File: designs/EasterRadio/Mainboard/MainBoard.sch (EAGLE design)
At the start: 83 parts, among them IC1 74HC595D, IC2 74HC595D, IC3 74HC595D, IC4 Analog Digital, IC6 CP2102, Q1 SS8050-G, Q2 SS8050-G

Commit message: checked Mainboard and esp32
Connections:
- net 3.3V: no longer GPIOS.5
- net CS2: now also GPIOS.5
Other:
- note added: "Mainboard"
- note added: "Revision 1 02.04.21"
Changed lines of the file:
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@@
 <plain>
 <frame x1="0" y1="0" x2="370.84" y2="337.82" columns="8" rows="5" layer="91"/>
+<text x="2.54" y="340.36" size="6.4516" layer="91">Mainboard</text>
+<text x="48.26" y="340.36" size="1.778" layer="91">Revision 1 02.04.21</text>
 </plain>
 <instances>
@@
 </instances>
 <busses>
-<bus name="SPI:CS,CS2,DC,GND,MOSI,RST,SCLK,SDA">
+<bus name="SPI:CS,DC,GND,MOSI,RST,SCLK,SDA">
 <segment>
 <wire x1="157.48" y1="177.8" x2="157.48" y2="154.94" width="0.762" layer="92"/>
@@
 <label x="218.44" y="96.52" size="1.778" layer="95"/>
 <pinref part="GPIOS" gate="A" pin="4"/>
-<pinref part="GPIOS" gate="A" pin="5"/>
-<wire x1="238.76" y1="93.98" x2="218.44" y2="93.98" width="0.1524" layer="91"/>
-<wire x1="218.44" y1="93.98" x2="218.44" y2="96.52" width="0.1524" layer="91"/>
-<pinref part="GPIOS" gate="A" pin="6"/>
-<wire x1="238.76" y1="91.44" x2="218.44" y2="91.44" width="0.1524" layer="91"/>
-<wire x1="218.44" y1="91.44" x2="218.44" y2="93.98" width="0.1524" layer="91"/>
-<junction x="218.44" y="93.98"/>
 </segment>
 <segment>
@@
 <label x="254" y="55.88" size="1.778" layer="95" rot="R90"/>
 <pinref part="AMPLIFIER" gate="A" pin="8"/>
+</segment>
+<segment>
+<pinref part="GPIOS" gate="A" pin="6"/>
+<wire x1="238.76" y1="91.44" x2="218.44" y2="91.44" width="0.1524" layer="91"/>
+<label x="218.44" y="91.44" size="1.778" layer="95"/>
 </segment>
 </net>
@@
 <segment>
 <pinref part="ESP32" gate="A" pin="10"/>
-<wire x1="180.34" y1="144.78" x2="213.36" y2="144.78" width="0.1524" layer="91"/>
+<wire x1="180.34" y1="144.78" x2="200.66" y2="144.78" width="0.1524" layer="91"/>
 <label x="200.66" y="144.78" size="1.778" layer="95" align="bottom-right"/>
-<wire x1="213.36" y1="144.78" x2="215.9" y2="142.24" width="0.1524" layer="91"/>
 </segment>
 <segment>
@@
 <label x="276.86" y="154.94" size="1.778" layer="95"/>
 </segment>
+<segment>
+<pinref part="GPIOS" gate="A" pin="5"/>
+<wire x1="238.76" y1="93.98" x2="218.44" y2="93.98" width="0.1524" layer="91"/>
+<label x="218.44" y="93.98" size="1.778" layer="95"/>
+</segment>
 </net>

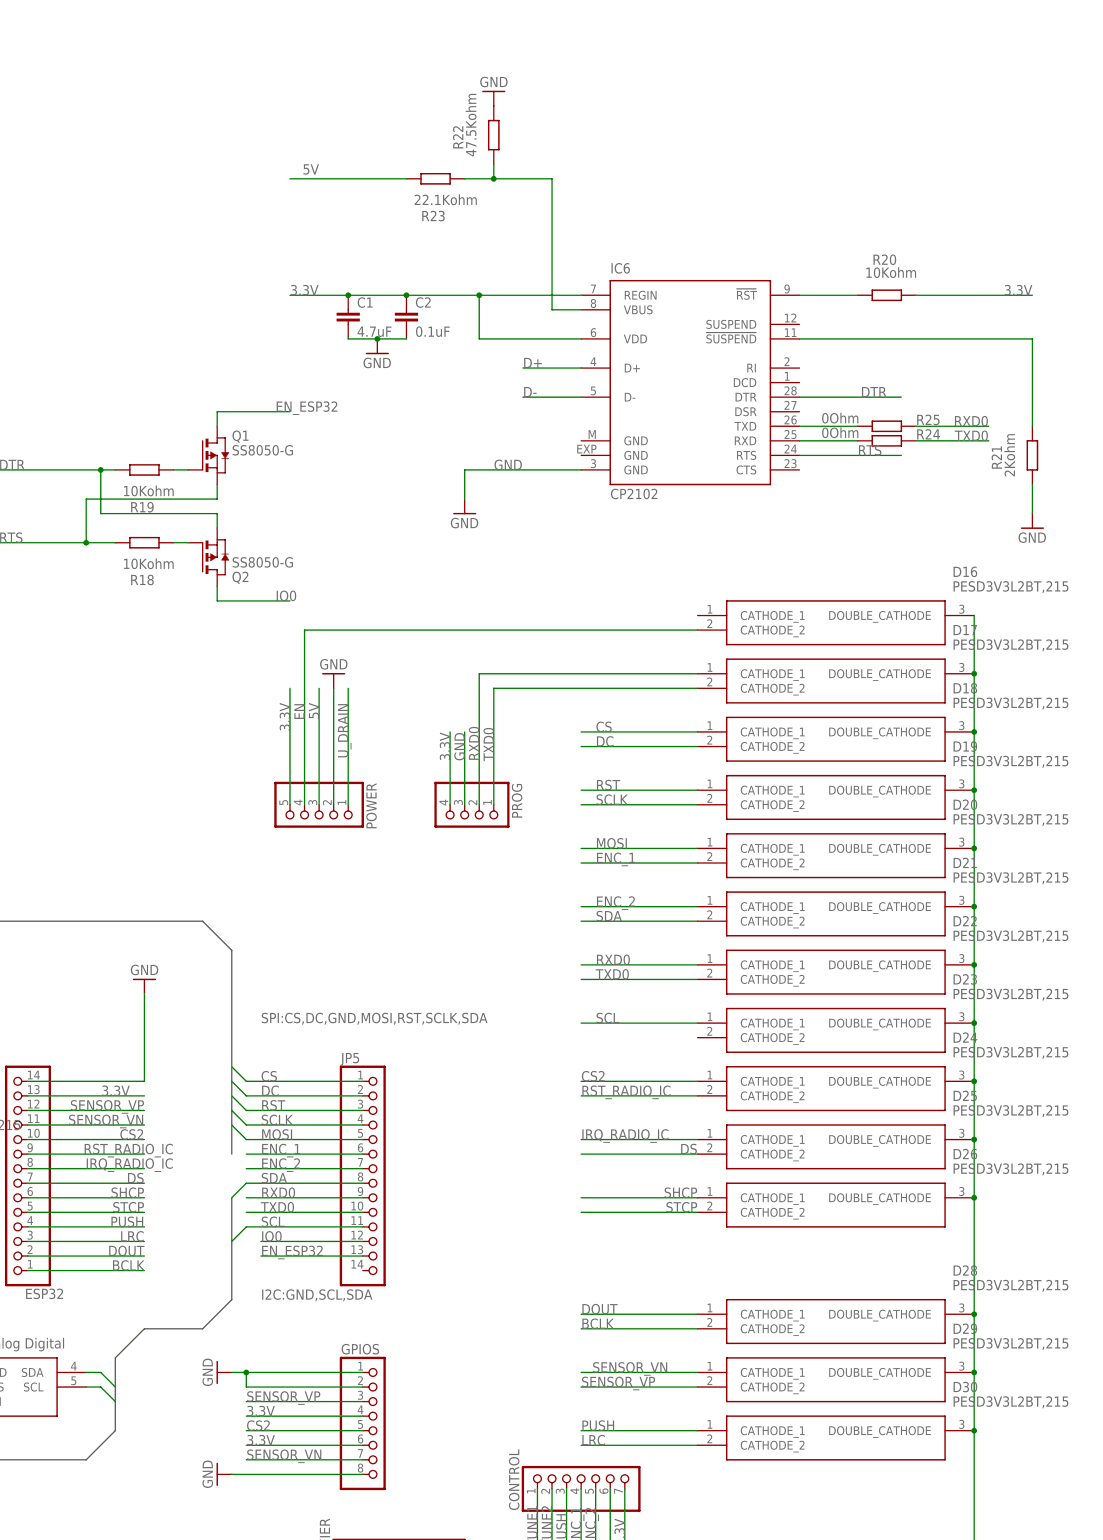
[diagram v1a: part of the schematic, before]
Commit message: small change to flsh chip for esp32
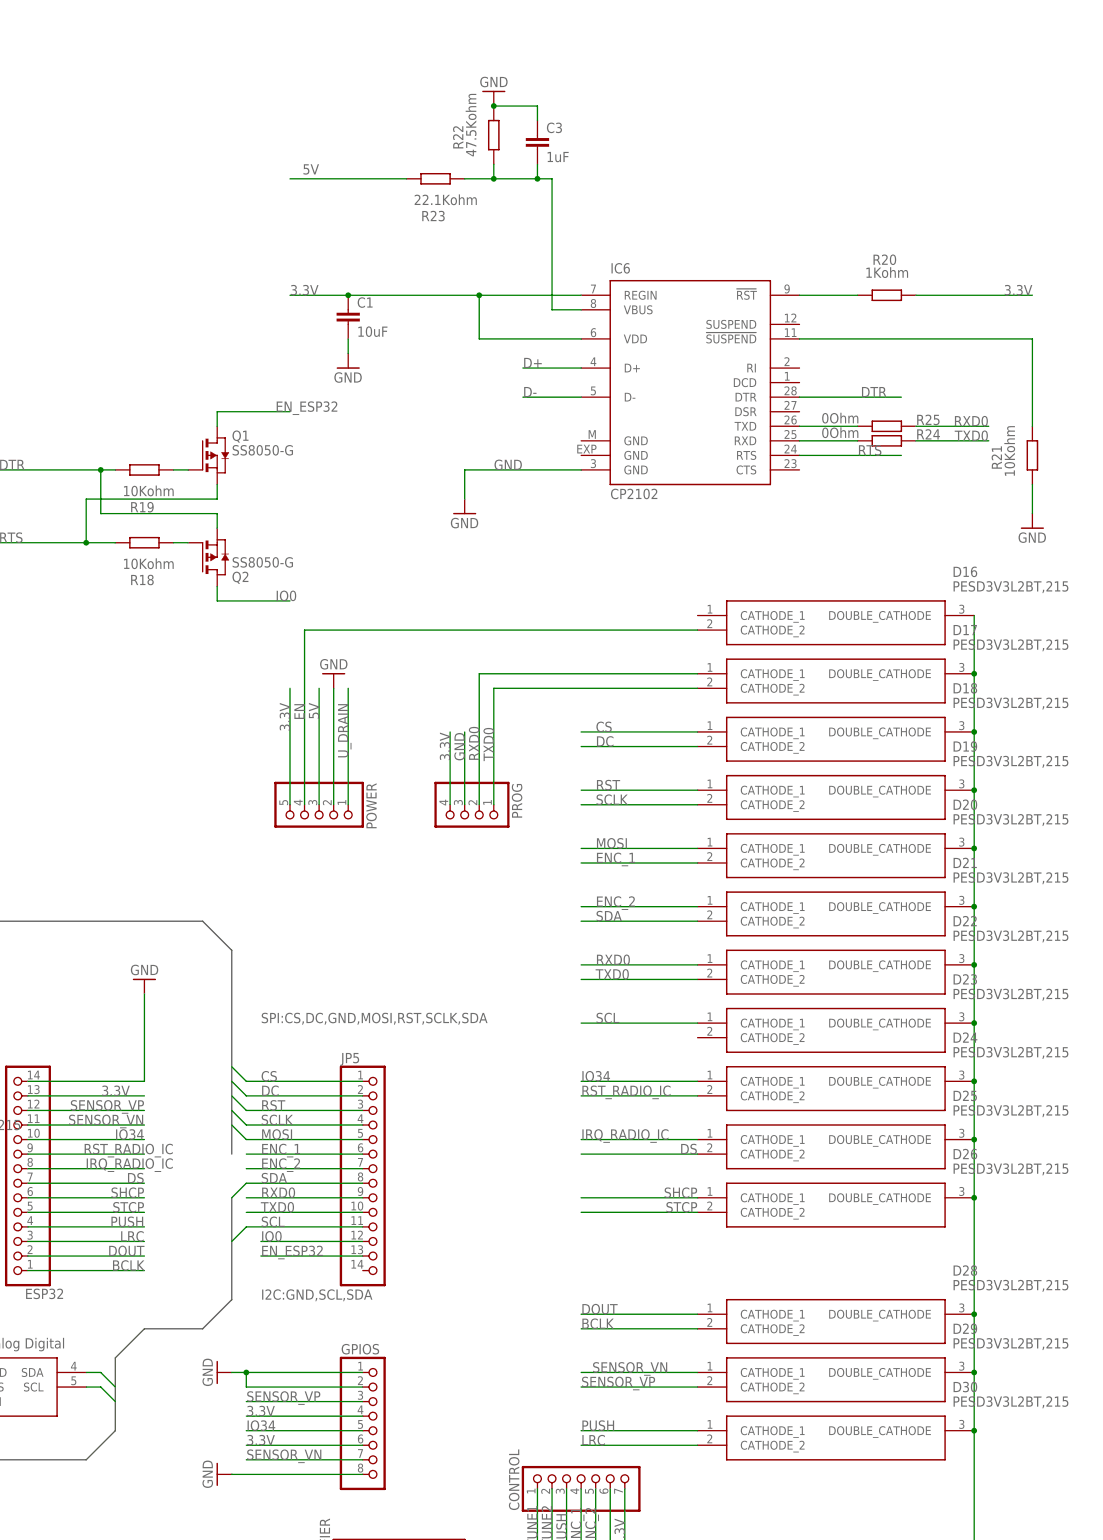
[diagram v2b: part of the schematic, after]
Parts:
- removed C2: 0.1uF, rcl:C-EUC0805
- added C3: 1uF, rcl:C-EUC0805
- C1: value 4.7uF -> 10uF
- R20: value 10Kohm -> 1Kohm
- R21: value 2Kohm -> 10Kohm
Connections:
- net CS2 renamed IO34
- net 3.3V: no longer C2.1
- net GND: now also C3.1; no longer C2.2
- net N$44: now also C3.2
